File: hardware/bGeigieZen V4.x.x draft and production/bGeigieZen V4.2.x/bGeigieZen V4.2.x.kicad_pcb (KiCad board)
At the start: 2 copper layers, 129.4 x 64.6 mm, 13 parts, among them J1 M5 2x15 pin, J3 GPS, J4 Geiger Safepulse, J5 Extra support header

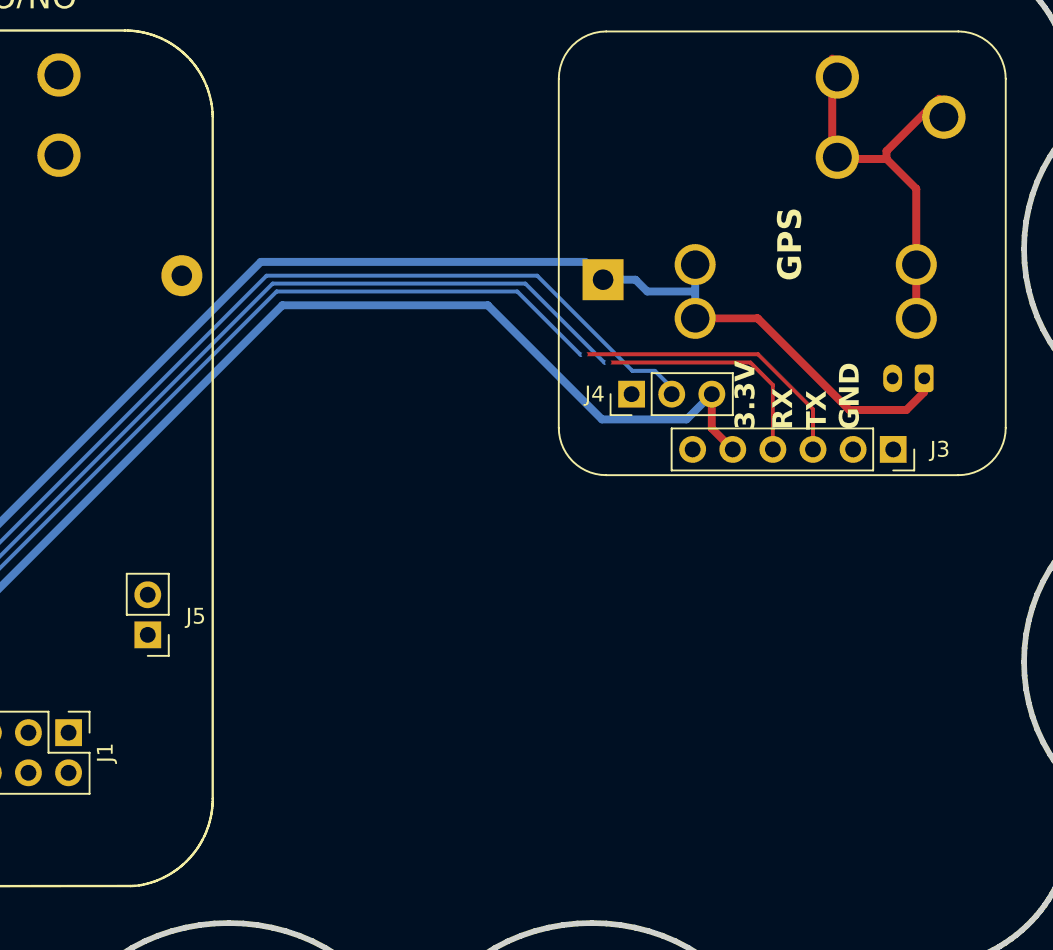
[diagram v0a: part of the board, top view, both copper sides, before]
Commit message: Changed V4.2.x board labeling
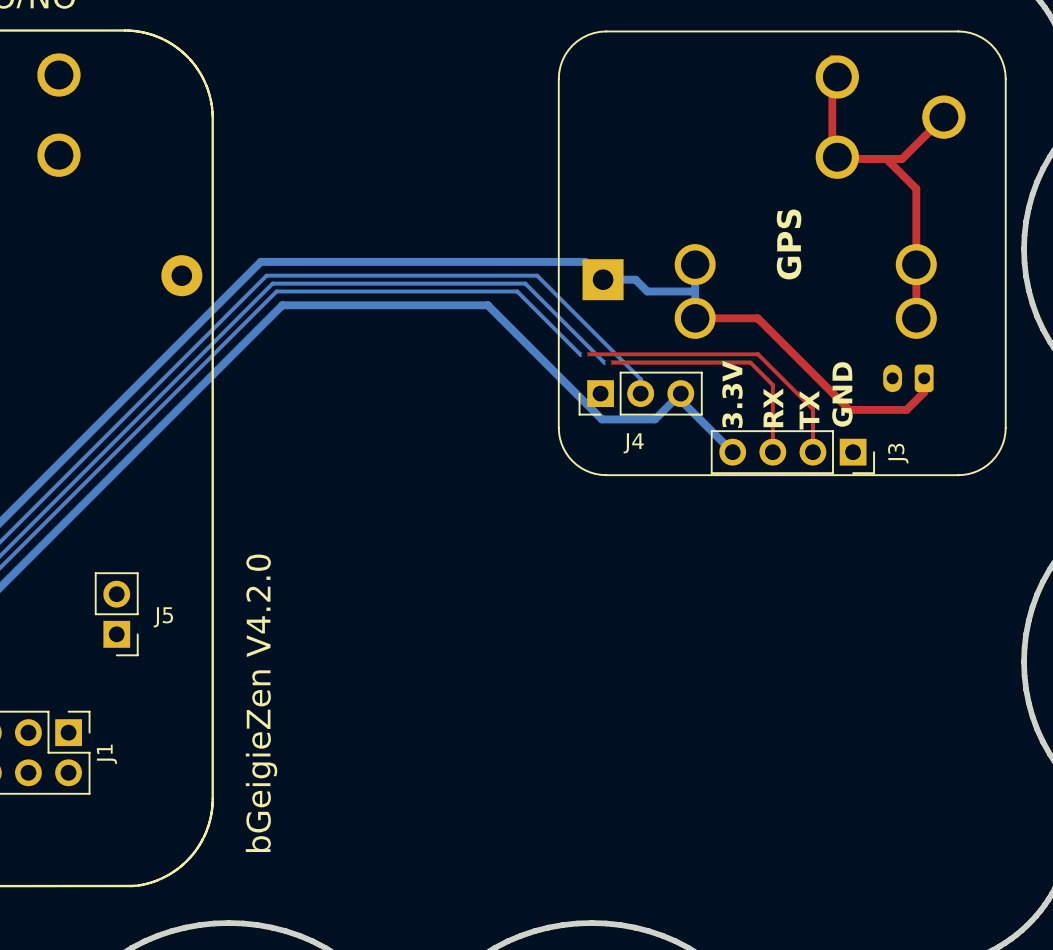
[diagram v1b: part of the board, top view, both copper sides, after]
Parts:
- J3: footprint Connector_PinSocket_2.54mm:PinSocket_1x06_P2.54mm_Vertical -> Connector_PinSocket_2.54mm:PinSocket_1x04_P2.54mm_Vertical
- moved J3 2.55 mm to (200.3, 98.7)
- moved J4 1.97 mm to (184.3, 95.0)
- moved J5 1.97 mm to (153.7, 110.2)
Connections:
- J3 pad 1: unconnected-(J3-Pin_1-Pad1) -> GND
- J3 pad 2: GND -> /TX2
- J3 pad 3: /TX2 -> /RX2
- J3 pad 4: /RX2 -> 3.3V
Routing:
- net /GIO2 on Core and GIO32 on Core-2: track 78.1 -> 76.4 mm
- net 3.3V: track 73.0 -> 72.4 mm
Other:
- board text added: "+3.3V"
- board text added: "Pulse"

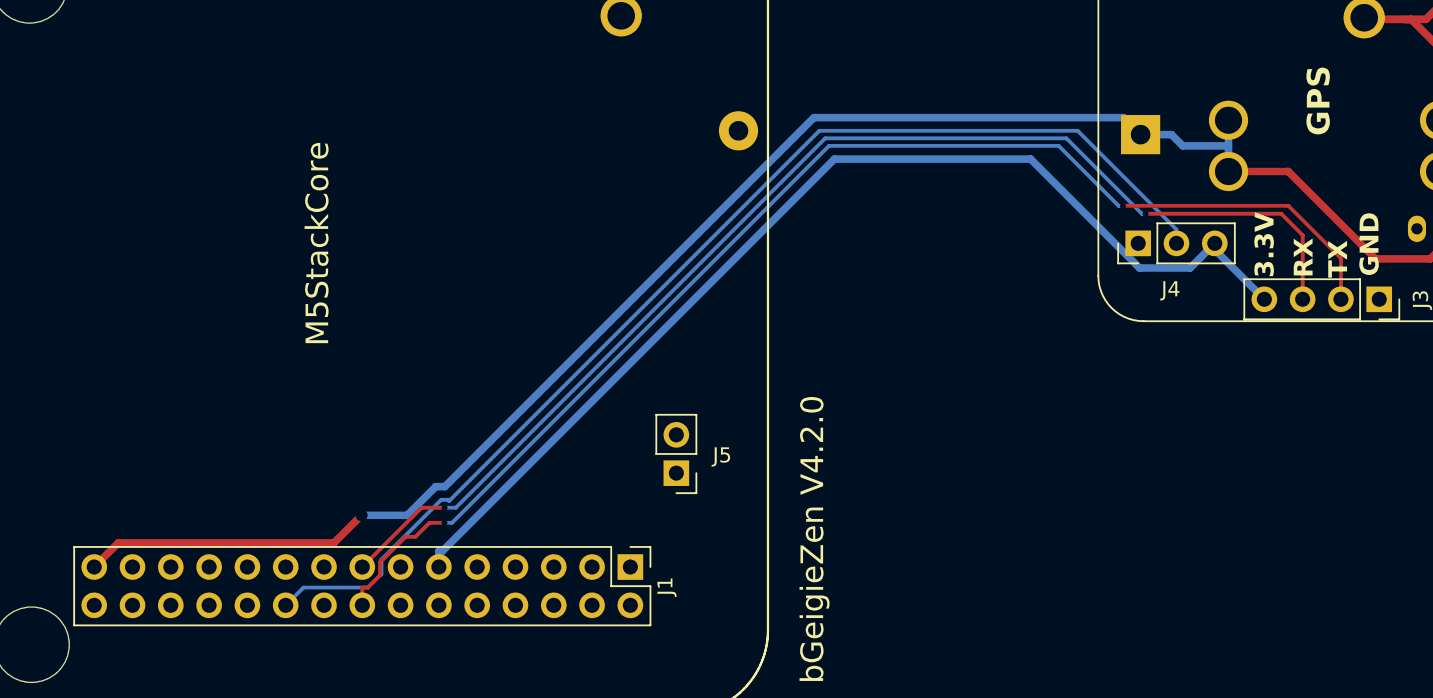
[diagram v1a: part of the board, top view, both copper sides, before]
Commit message: Update V4.2.0 boards and V5.x.x. boards
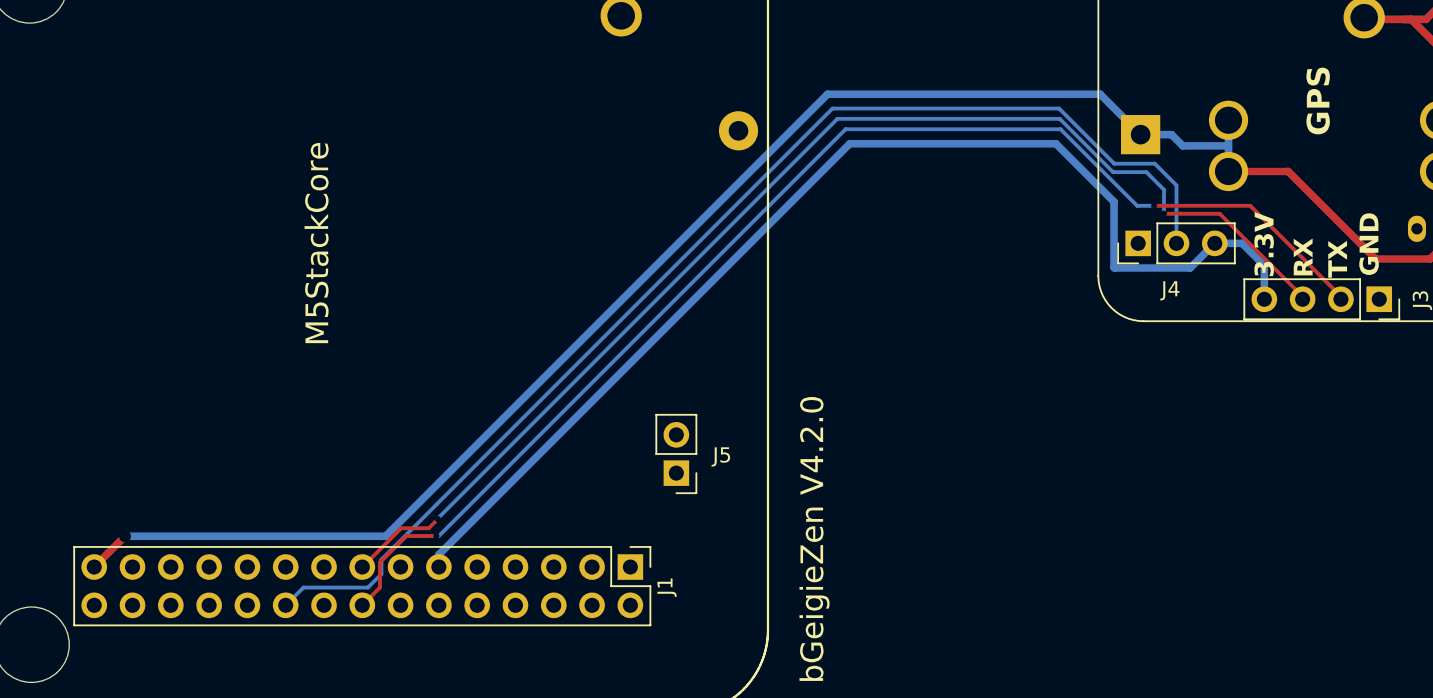
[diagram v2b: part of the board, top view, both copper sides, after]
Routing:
- net 3.3V: track 72.4 -> 76.8 mm
- net /GIO2 on Core and GIO32 on Core-2: track 76.4 -> 79.2 mm
- net /BAT: track 110.0 -> 111.3 mm
- net /TX2: track 84.4 -> 83.6 mm
